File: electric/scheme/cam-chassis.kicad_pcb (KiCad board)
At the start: 2 copper layers, 51.5 x 28.5 mm, 48 parts, among them IC1 ATMEGA8-AI, K1 pyro, P1 TST, P2 TST, P3 TST, P4 TST, P5 TST, P6 TST, P7 servo, Q3 bc857, Q4 bc847, Q5 irlml2244, Q6 NPN, Q7 irlml2244, U1 crystal-4pin, U2 MICRO-USB-B

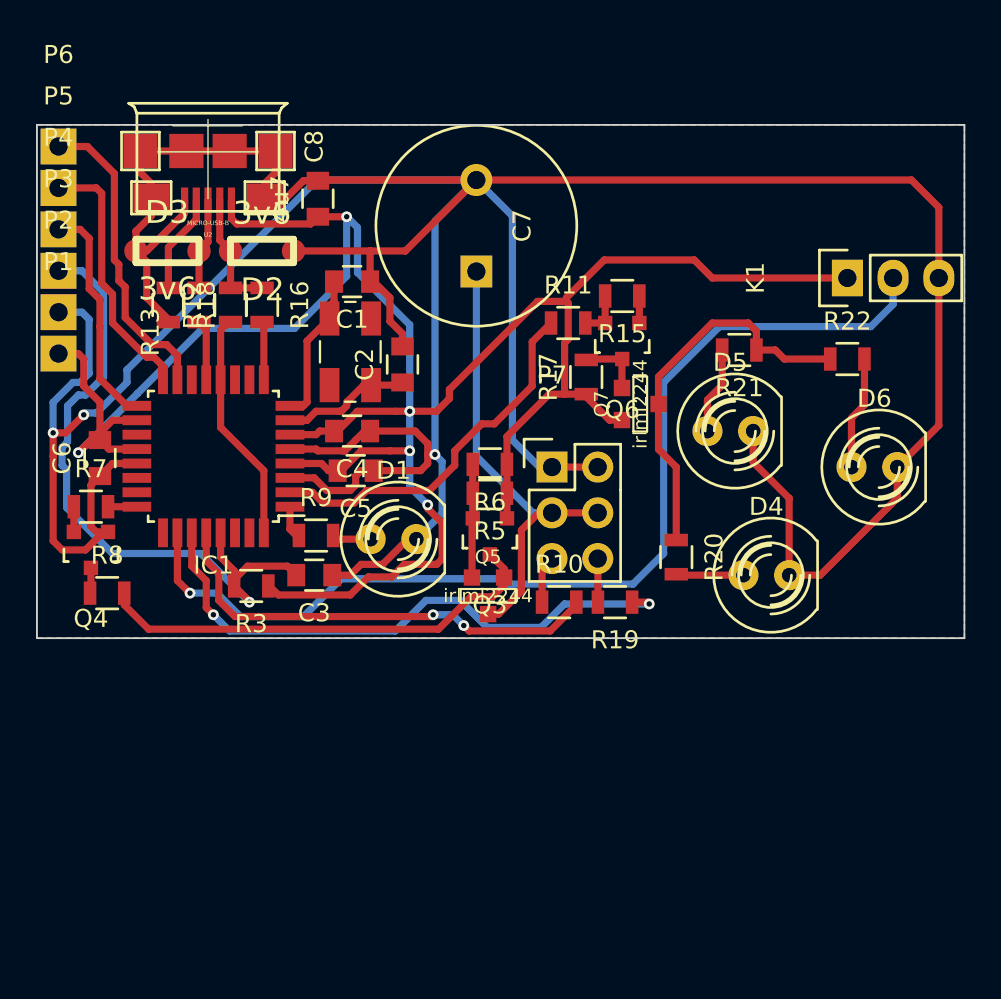
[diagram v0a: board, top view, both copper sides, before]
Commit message: Replaced components to the ones I have.
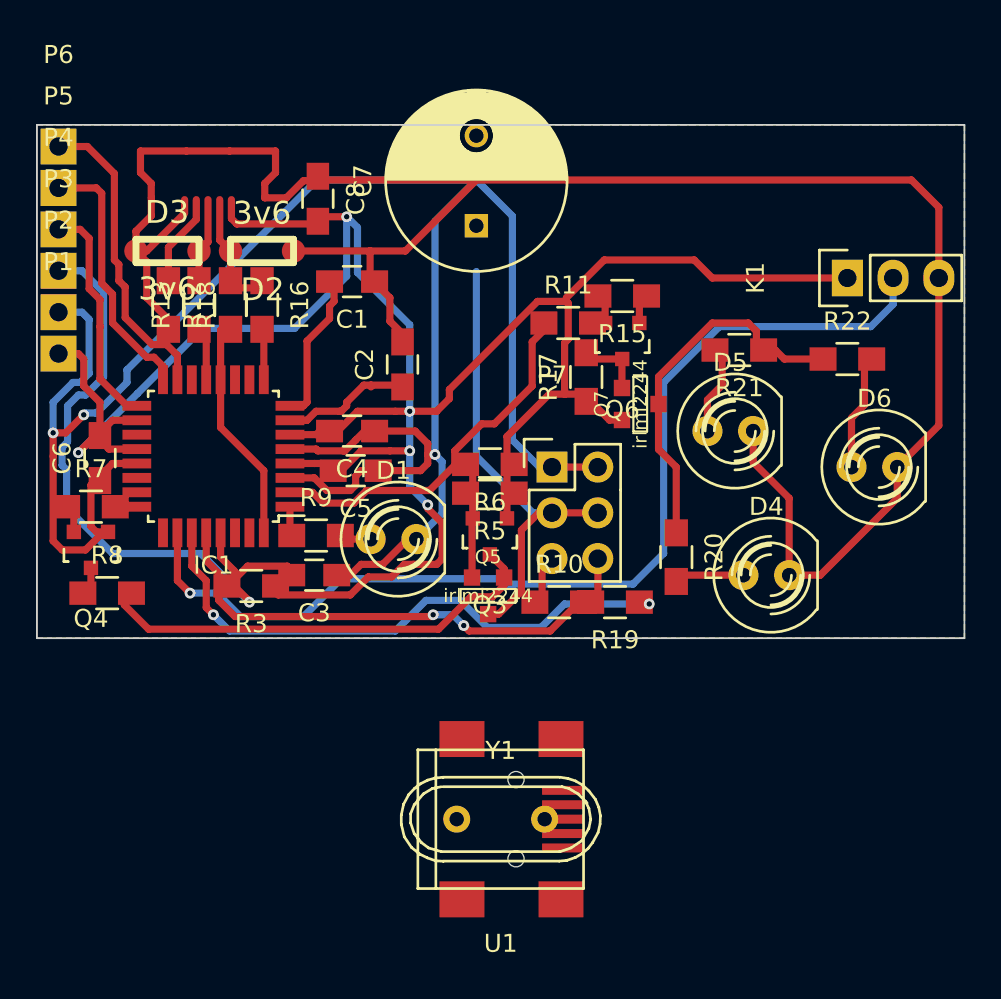
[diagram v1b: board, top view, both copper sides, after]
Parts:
- removed U2: MICRO-USB-B, micro-usb-b:micro-usb-b
- added Y1: Crystal, Crystals:Crystal_HC49-U_Vertical, F.Cu at (124.2, 122.6)
- C1, C2, C3, C4, C5, C6, C8: footprint Capacitors_SMD:C_0805 -> Capacitors_SMD:C_0805_HandSoldering
- C7: footprint Discret:C2V10 -> Capacitors_ThroughHole:C_Radial_D10_L13_P5
- R10, R11, R12, R13, R15, R16, R17, R18, R19, R20, R21, R22, R3, R5, R6, R7, R8, R9: footprint Resistors_SMD:R_0805 -> Resistors_SMD:R_0805_HandSoldering
- U1: value crystal-4pin -> MINI-USB-B-4-bases; footprint crystal-smd-5x3:CRYSTAL-SMD-5x3 -> Connect:USB_Mini-B
- moved U1 27.3 mm to (124.2, 122.6), turned to 0 degrees
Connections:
- U1 pad 1: /xtal2 -> VCC
- U1 pad 2: (no net) -> Net-(D2-Pad2)
- U1 pad 3: /xtal1 -> Net-(D3-Pad2)
- U1 pad 4: (no net) -> Net-(R18-Pad1)
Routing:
- net /led: track 20.8 -> 14.5 mm
- net /src: track 6.30 -> 12.6 mm
- net Net-(P7-Pad5): track 2.65 -> 7.84 mm
- net /servo-vcc: track 26.2 -> 21.0 mm
